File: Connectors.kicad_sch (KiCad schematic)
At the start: 13 parts, among them J1 GD820HTX75P6HB, J3 Control_A, J4 Control_C, J5 Control_B, Q1 IRLML2402TRPBF, Q2 IRLML2402TRPBF, Q3 IRLML2402TRPBF

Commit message: Исправления: заменил полевые на биполярные в контуре RESET и изменил номиналы резисторов базы, исправил BOM
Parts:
- removed Q1, Q2, Q3: IRLML2402TRPBF, Package_TO_SOT_SMD:SOT-23, symbol Transistor_FET:2N7002
- added Q1, Q2, Q3: BC817, Package_TO_SOT_SMD:SOT-23, symbol Device:Q_NPN_BEC
- R100, R102, R98: value 0 -> 4.7k
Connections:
- net GND: now also Q1.2 (E), Q2.2 (E), Q3.2 (E)
- net ~{RST_A}: now also Q2.3 (C)
- net ~{RST_B}: now also Q1.3 (C)
- net ~{RST_C}: now also Q3.3 (C)
- net at R102.2: now also Q3.1 (B)
- net at R100.2: now also Q1.1 (B)
- net at R98.2: now also Q2.1 (B)

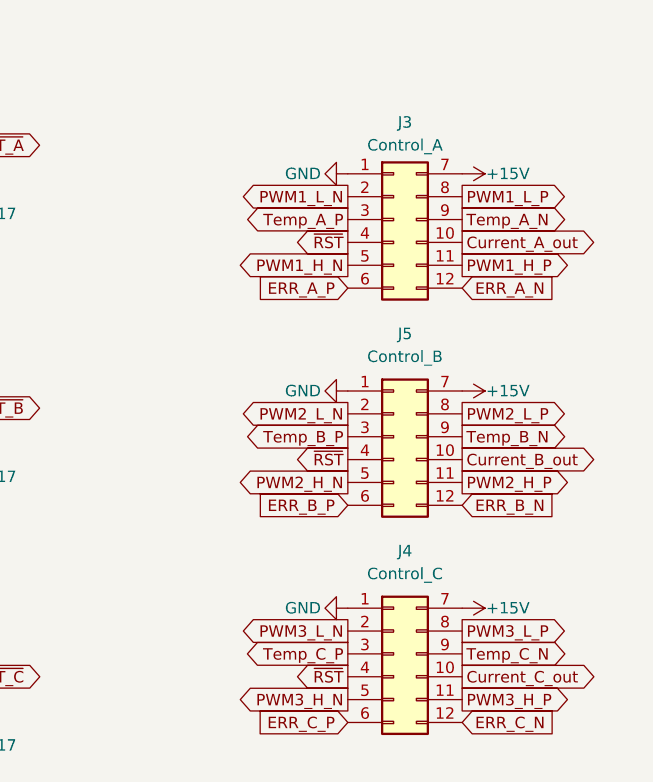
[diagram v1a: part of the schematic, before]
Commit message: VER2.1: переработал цепь DESAT
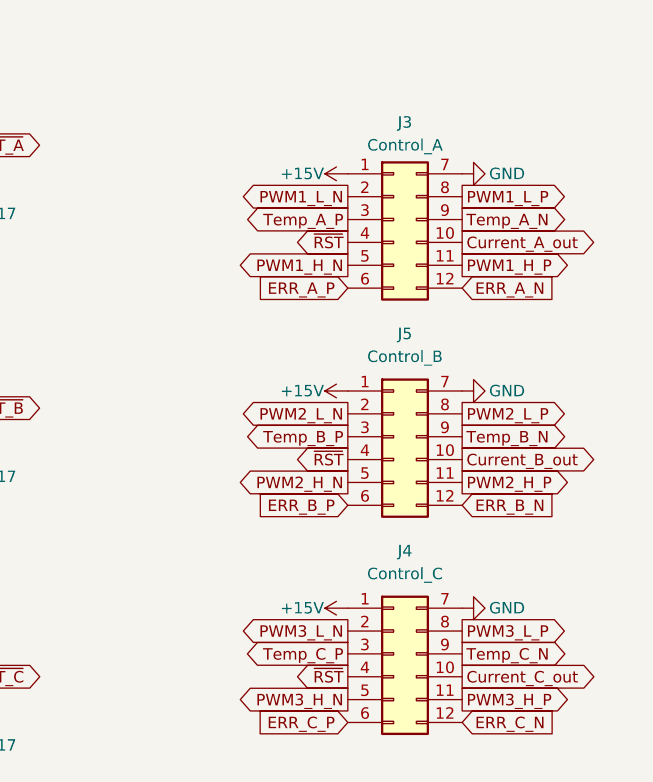
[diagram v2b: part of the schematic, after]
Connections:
- net +15V: now also J3.1 (Pin_1), J4.1 (Pin_1), J5.1 (Pin_1); no longer J3.7 (Pin_7), J4.7 (Pin_7), J5.7 (Pin_7)
- net GND: now also J3.7 (Pin_7), J4.7 (Pin_7), J5.7 (Pin_7); no longer J3.1 (Pin_1), J4.1 (Pin_1), J5.1 (Pin_1)
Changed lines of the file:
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@@
 	(symbol
 		(lib_id "power:GND")
-		(at 111.125 101.6 270)
+		(at 123.825 101.6 90)
 		(unit 1)
 		(exclude_from_sim no)
@@
 		(dnp no)
 		(property "Reference" "#PWR0134"
-			(at 104.775 101.6 0)
+			(at 130.175 101.6 0)
 			(effects
 				(font
@@
 		)
 		(property "Value" "GND"
-			(at 104.14 101.6 90)
+			(at 130.81 101.6 90)
 			(effects
 				(font
@@
 		)
 		(property "Footprint" ""
-			(at 111.125 101.6 0)
+			(at 123.825 101.6 0)
 			(effects
 				(font
@@
 		)
 		(property "Datasheet" ""
-			(at 111.125 101.6 0)
+			(at 123.825 101.6 0)
 			(effects
 				(font
@@
 		)
 		(property "Description" "Power symbol creates a global label with name \"GND\" , ground"
-			(at 111.125 101.6 0)
+			(at 123.825 101.6 0)
 			(effects
 				(font
@@
 	(symbol
 		(lib_id "power:GND")
-		(at 111.125 149.86 270)
+		(at 123.825 149.86 90)
 		(unit 1)
 		(exclude_from_sim no)
@@
 		(dnp no)
 		(property "Reference" "#PWR0219"
-			(at 104.775 149.86 0)
+			(at 130.175 149.86 0)
 			(effects
 				(font
@@
 		)
 		(property "Value" "GND"
-			(at 104.14 149.86 90)
+			(at 130.81 149.86 90)
 			(effects
 				(font
@@
 		)
 		(property "Footprint" ""
-			(at 111.125 149.86 0)
+			(at 123.825 149.86 0)
 			(effects
 				(font
@@
 		)
 		(property "Datasheet" ""
-			(at 111.125 149.86 0)
+			(at 123.825 149.86 0)
 			(effects
 				(font
@@
 		)
 		(property "Description" "Power symbol creates a global label with name \"GND\" , ground"
-			(at 111.125 149.86 0)
+			(at 123.825 149.86 0)
 			(effects
 				(font
@@
 	(symbol
 		(lib_id "power:+15V")
-		(at 123.825 149.86 270)
+		(at 111.125 149.86 90)
 		(unit 1)
 		(exclude_from_sim no)
@@
 		(dnp no)
 		(property "Reference" "#PWR0221"
-			(at 120.015 149.86 0)
+			(at 114.935 149.86 0)
 			(effects
 				(font
@@
 		)
 		(property "Value" "+15V"
-			(at 128.905 149.86 90)
+			(at 106.045 149.86 90)
 			(effects
 				(font
@@
 		)
 		(property "Footprint" ""
-			(at 123.825 149.86 0)
+			(at 111.125 149.86 0)
 			(effects
 				(font
@@
 		)
 		(property "Datasheet" ""
-			(at 123.825 149.86 0)
+			(at 111.125 149.86 0)
 			(effects
 				(font
@@
 		)
 		(property "Description" "Power symbol creates a global label with name \"+15V\""
-			(at 123.825 149.86 0)
+			(at 111.125 149.86 0)
 			(effects
 				(font
@@
 	(symbol
 		(lib_id "power:+15V")
-		(at 123.825 125.73 270)
+		(at 111.125 125.73 90)
 		(unit 1)
 		(exclude_from_sim no)
@@
 		(dnp no)
 		(property "Reference" "#PWR0220"
-			(at 120.015 125.73 0)
+			(at 114.935 125.73 0)
 			(effects
 				(font
@@
 		)
 		(property "Value" "+15V"
-			(at 128.905 125.73 90)
+			(at 106.045 125.73 90)
 			(effects
 				(font
@@
 		)
 		(property "Footprint" ""
-			(at 123.825 125.73 0)
+			(at 111.125 125.73 0)
 			(effects
 				(font
@@
 		)
 		(property "Datasheet" ""
-			(at 123.825 125.73 0)
+			(at 111.125 125.73 0)
 			(effects
 				(font
@@
 		)
 		(property "Description" "Power symbol creates a global label with name \"+15V\""
-			(at 123.825 125.73 0)
+			(at 111.125 125.73 0)
 			(effects
 				(font
@@
 	(symbol
 		(lib_id "power:GND")
-		(at 111.125 125.73 270)
+		(at 123.825 125.73 90)
 		(unit 1)
 		(exclude_from_sim no)
@@
 		(dnp no)
 		(property "Reference" "#PWR0133"
-			(at 104.775 125.73 0)
+			(at 130.175 125.73 0)
 			(effects
 				(font
@@
 		)
 		(property "Value" "GND"
-			(at 104.14 125.73 90)
+			(at 130.81 125.73 90)
 			(effects
 				(font
@@
 		)
 		(property "Footprint" ""
-			(at 111.125 125.73 0)
+			(at 123.825 125.73 0)
 			(effects
 				(font
@@
 		)
 		(property "Datasheet" ""
-			(at 111.125 125.73 0)
+			(at 123.825 125.73 0)
 			(effects
 				(font
@@
 		)
 		(property "Description" "Power symbol creates a global label with name \"GND\" , ground"
-			(at 111.125 125.73 0)
+			(at 123.825 125.73 0)
 			(effects
 				(font
@@
 	(symbol
 		(lib_id "power:+15V")
-		(at 123.825 101.6 270)
+		(at 111.125 101.6 90)
 		(unit 1)
 		(exclude_from_sim no)
@@
 		(dnp no)
 		(property "Reference" "#PWR0135"
-			(at 120.015 101.6 0)
+			(at 114.935 101.6 0)
 			(effects
 				(font
@@
 		)
 		(property "Value" "+15V"
-			(at 128.905 101.6 90)
+			(at 106.045 101.6 90)
 			(effects
 				(font
@@
 		)
 		(property "Footprint" ""
-			(at 123.825 101.6 0)
+			(at 111.125 101.6 0)
 			(effects
 				(font
@@
 		)
 		(property "Datasheet" ""
-			(at 123.825 101.6 0)
+			(at 111.125 101.6 0)
 			(effects
 				(font
@@
 		)
 		(property "Description" "Power symbol creates a global label with name \"+15V\""
-			(at 123.825 101.6 0)
-			(effects
-				(font
+			(at 111.125 101.6 0)
+			(effects
+				(font

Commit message: VER2.2: все изменения в списке изменений
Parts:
- J1: value GD820HTX75P6HB -> ~; Product Name (none) -> GD820HTX75P6HB
- J3: value Control_A -> ~; Description P/N (none) -> Connector; Purpose (none) -> Control_A
- J4: value Control_C -> ~; Description P/N (none) -> Connector; Purpose (none) -> Control_C
- J5: value Control_B -> ~; Description P/N (none) -> Connector; Purpose (none) -> Control_B
- Q1, Q2, Q3: value BC817 -> ~; Description P/N (none) -> Bipolar transistor; Product Name (none) -> BC817
